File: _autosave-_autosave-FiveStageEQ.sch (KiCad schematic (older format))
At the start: 75 parts, among them J1 AudioJack3, J2 AudioJack3, U1 LM833, U2 LM833, U3 LM833, U4 LM833, U5 LM833, U6 LM833, U7 LM833, U8 LM317_TO3

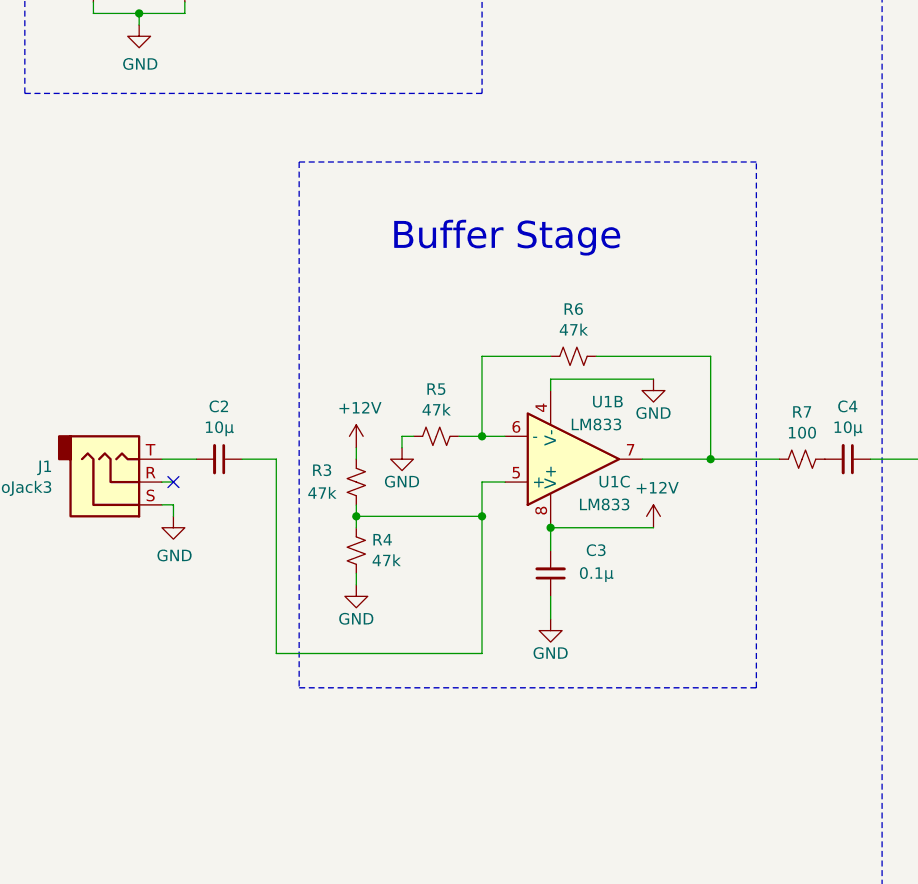
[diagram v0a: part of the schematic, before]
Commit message: Corrected schematic
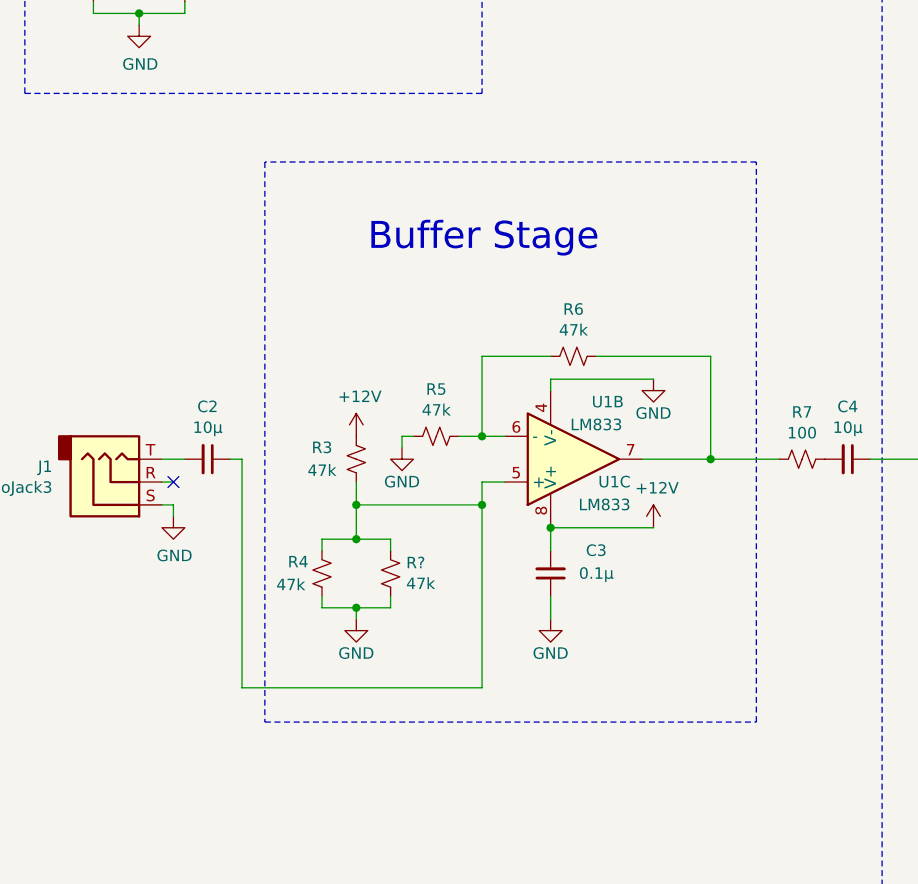
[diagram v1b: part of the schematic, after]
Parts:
- added R?: 47k, Resistor_SMD:R_0603_1608Metric, symbol FiveStageEQ-rescue:R_Small_US-Device
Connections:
- net GND: now also R?.1
- net at C2.1, R3.2, R4.2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: now also R?.2
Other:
- moved on the sheet: C2, R3, R4

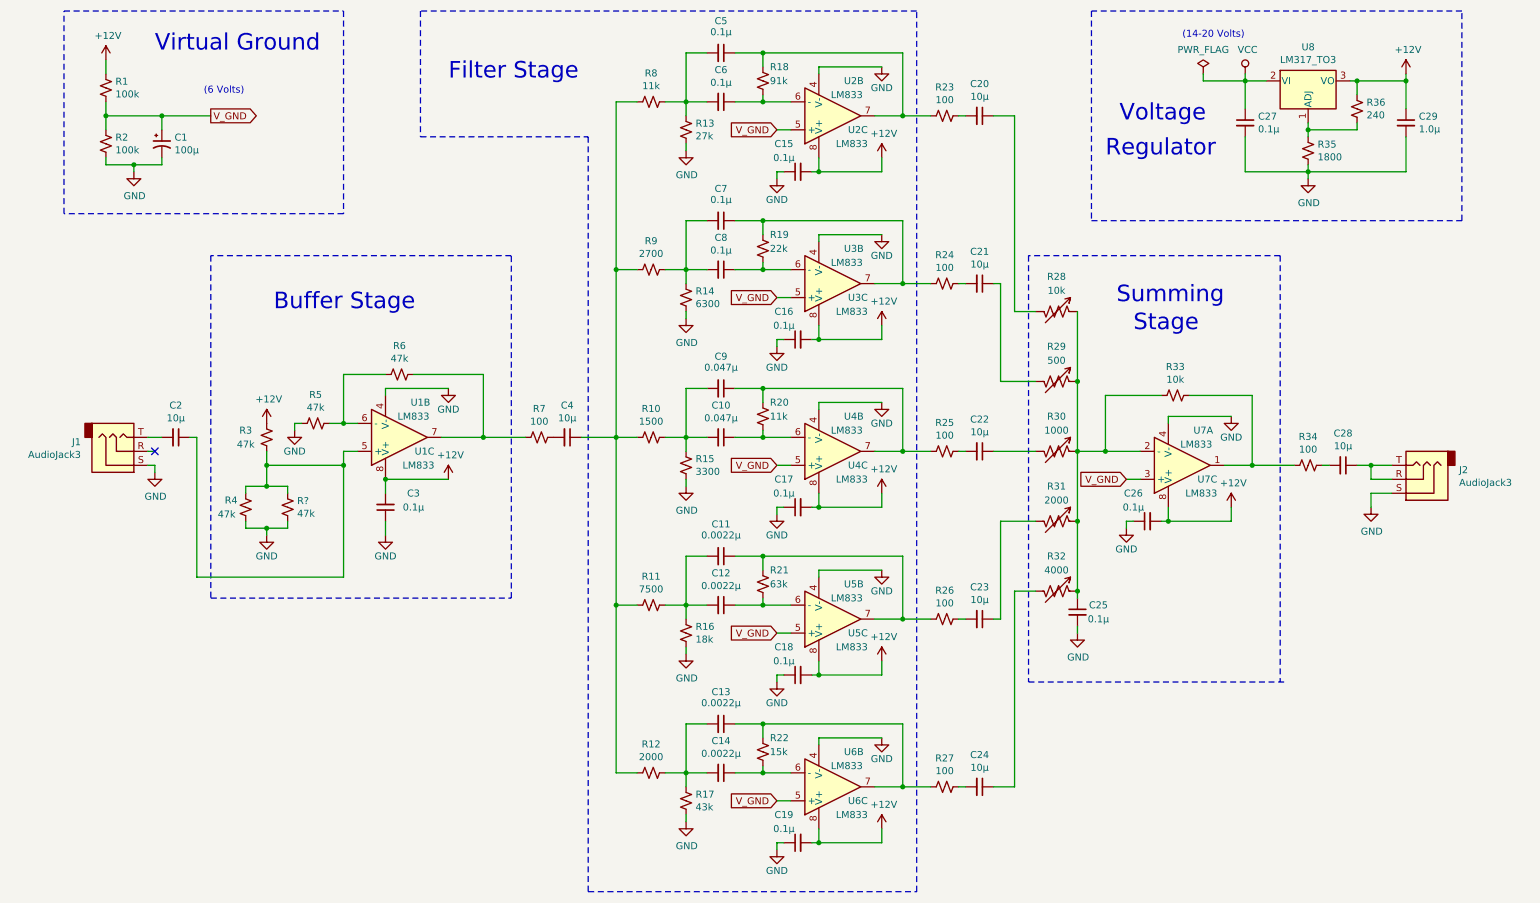
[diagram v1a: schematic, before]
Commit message: added poster of EQ
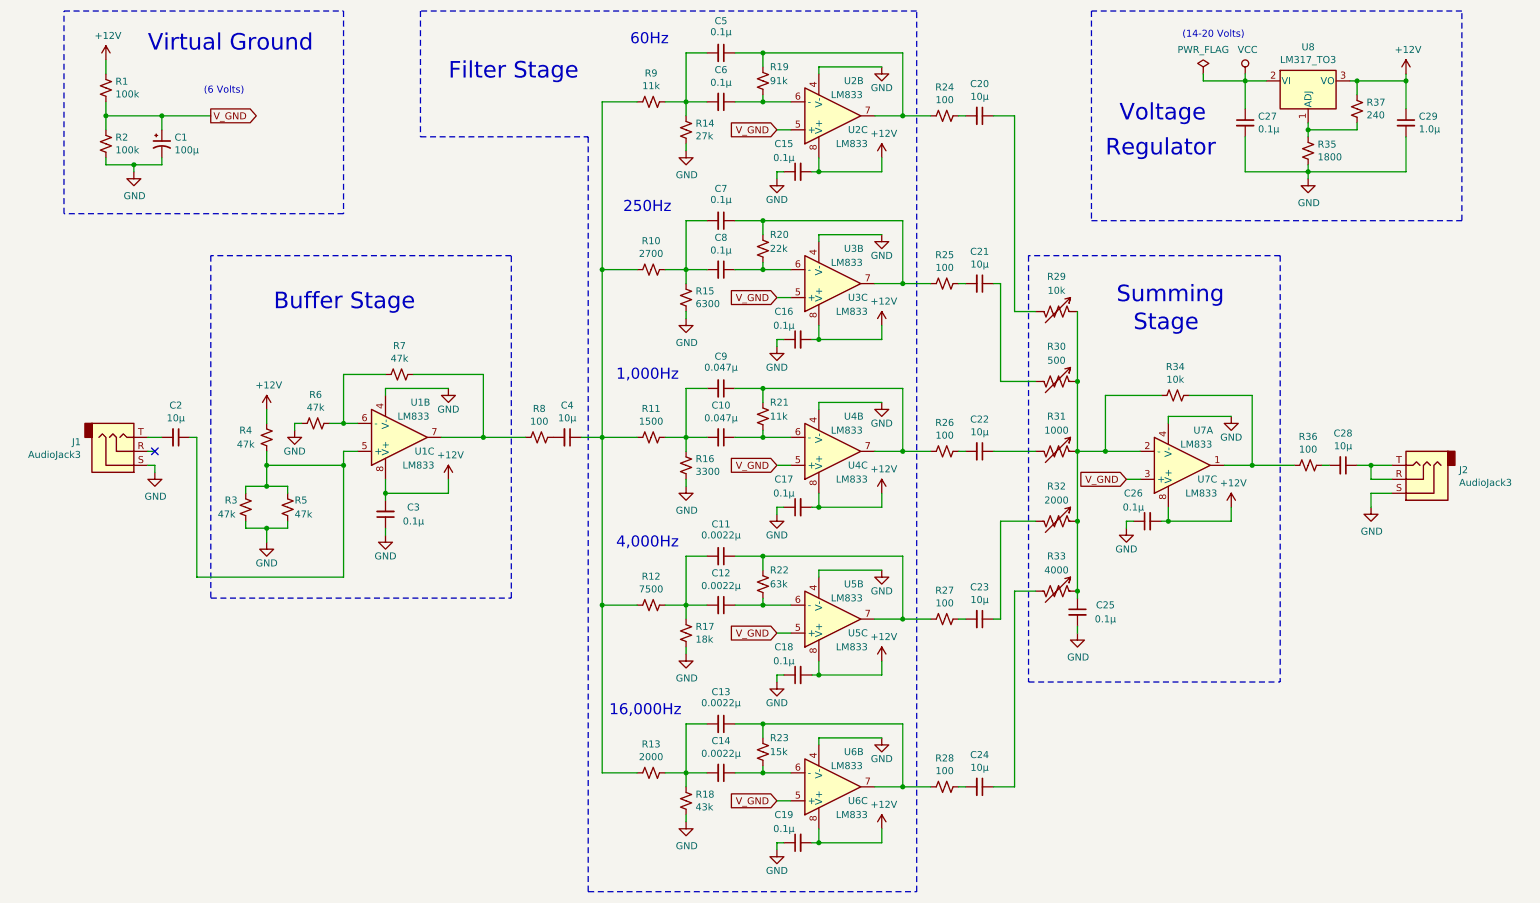
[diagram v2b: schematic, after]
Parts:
- removed R?: 47k, Resistor_SMD:R_0603_1608Metric, symbol FiveStageEQ-rescue:R_Small_US-Device
- added R5: 47k, Resistor_SMD:R_0603_1608Metric, symbol FiveStageEQ-rescue:R_Small_US-Device
- renumbered R9 to R10, R10 to R11, R11 to R12, R12 to R13, R13 to R14, R14 to R15, R15 to R16, R16 to R17, R17 to R18, R18 to R19, R19 to R20, R20 to R21, R21 to R22, R22 to R23, R23 to R24, R24 to R25, R25 to R26, R26 to R27, R27 to R28, R28 to R29, R4 to R3, R29 to R30, R30 to R31, R31 to R32, R32 to R33, R33 to R34, R34 to R36, R36 to R37, R3 to R4, R5 to R6, R6 to R7, R7 to R8, R8 to R9
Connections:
- net GND: now also R5.1
- net at C2.1, R3.2, R4.2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: now also R5.2
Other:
- note added: "1,000Hz"
- note added: "16,000Hz"
- note added: "250Hz"
- note added: "4,000Hz"
- note added: "60Hz"
- moved on the sheet: C3

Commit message: added PCB design and made some adjustments to schematic to accomodate footprints
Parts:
- removed C16, C18: 0.1μ, Capacitor_SMD:C_0603_1608Metric, symbol FiveStageEQ-rescue:C_Small-Device
- removed J1, J2: AudioJack3, Connector_Audio:Jack_3.5mm_CUI_SJ-3523-SMT_Horizontal, symbol FiveStageEQ-rescue:AudioJack3-Connector
- removed R29: 10k, Potentiometer_THT:Potentiometer_Vishay_148-149_Single_Vertical, symbol FiveStageEQ-rescue:R_Variable_US-Device
- removed R30: 500, Potentiometer_THT:Potentiometer_Vishay_148-149_Single_Vertical, symbol FiveStageEQ-rescue:R_Variable_US-Device
- removed R31: 1000, Potentiometer_THT:Potentiometer_Vishay_148-149_Single_Vertical, symbol FiveStageEQ-rescue:R_Variable_US-Device
- removed R32: 2000, Potentiometer_THT:Potentiometer_Vishay_148-149_Single_Vertical, symbol FiveStageEQ-rescue:R_Variable_US-Device
- removed R33: 4000, Potentiometer_THT:Potentiometer_Vishay_148-149_Single_Vertical, symbol FiveStageEQ-rescue:R_Variable_US-Device
- removed unit 3 of U3
- removed unit 3 of U5
- added J1, J2: AudioJack3, SJ1-3523N:CUI_SJ1-3523N, symbol Connector:AudioJack3
- added R29: 10k, SamacSys_Parts:PTV09A4015FA103, symbol Device:R_Potentiometer_US
- added R30: 500, SamacSys_Parts:PCW1DC24BAB501L, symbol Device:R_Potentiometer_US
- added R31: 1000, SamacSys_Parts:PTV09A4015FB103, symbol Device:R_Potentiometer_US
- added R32: 2000, SamacSys_Parts:PTV09A4020FB503, symbol Device:R_Potentiometer_US
- added R33: 4000, SamacSys_Parts:PTV09A4020FB103, symbol Device:R_Potentiometer_US
- C1: footprint Capacitor_SMD:C_0603_1608Metric -> 100uf_cap:FK20X5R0J107M
- C10, C9: footprint Capacitor_SMD:C_0603_1608Metric -> SamacSys_Parts:CAPC1005X55N
- C11, C12, C13, C14: footprint Capacitor_SMD:C_0603_1608Metric -> SamacSys_Parts:CAPC0603X33N
- C15, C3, C5, C6, C7, C8: footprint Capacitor_SMD:C_0603_1608Metric -> SamacSys_Parts:CAPPA1472W54L508D241
- C16: renamed from C17; footprint Capacitor_SMD:C_0603_1608Metric -> SamacSys_Parts:CAPPA1472W54L508D241
- C17: renamed from C19; footprint Capacitor_SMD:C_0603_1608Metric -> SamacSys_Parts:CAPPA1472W54L508D241
- C18: renamed from C20; footprint Capacitor_SMD:C_0603_1608Metric -> SamacSys_Parts:RCE5C1H104J2A2H03B
- C19: renamed from C21; footprint Capacitor_SMD:C_0603_1608Metric -> SamacSys_Parts:RCE5C1H104J2A2H03B
- C2, C4: footprint Capacitor_SMD:C_0603_1608Metric -> SamacSys_Parts:RCE5C1H104J2A2H03B
- C20: renamed from C22; footprint Capacitor_SMD:C_0603_1608Metric -> SamacSys_Parts:RCE5C1H104J2A2H03B
- C21: renamed from C23; footprint Capacitor_SMD:C_0603_1608Metric -> SamacSys_Parts:RCE5C1H104J2A2H03B
- C22: renamed from C24; footprint Capacitor_SMD:C_0603_1608Metric -> SamacSys_Parts:RCE5C1H104J2A2H03B
- C23: renamed from C25; footprint Capacitor_SMD:C_0603_1608Metric -> SamacSys_Parts:CAPPA1472W54L508D241
- C24: renamed from C26; footprint Capacitor_SMD:C_0603_1608Metric -> SamacSys_Parts:CAPPA1472W54L508D241
- C25: renamed from C27; footprint Capacitor_SMD:C_0603_1608Metric -> SamacSys_Parts:CAPPA1472W54L508D241
- C26: renamed from C28; footprint Capacitor_SMD:C_0603_1608Metric -> SamacSys_Parts:RCE5C1H104J2A2H03B
- C27: renamed from C29; footprint Capacitor_SMD:C_0603_1608Metric -> SamacSys_Parts:C330C105K5R5TA
- R1, R10, R13, R14, R2, R22, R35: footprint Resistor_SMD:R_0603_1608Metric -> SamacSys_Parts:RESC2012X60N
- R11, R12, R15, R16, R18, R19, R20, R21, R23, R34, R37: footprint Resistor_SMD:R_0603_1608Metric -> SamacSys_Parts:RESC1608X55N
- R17: footprint Resistor_SMD:R_0603_1608Metric -> footprints:CFR-25JB-52-18K
- R24, R25, R26, R27, R28, R36, R8: footprint Resistor_SMD:R_0603_1608Metric -> SamacSys_Parts:RESAD2990W85L1150D460
- R3, R4, R5, R6, R7: footprint Resistor_SMD:R_0603_1608Metric -> footprints:RN73R1ETTP2001D25
- R9: footprint Resistor_SMD:R_0603_1608Metric -> SamacSys_Parts:RCE5C1H104J2A2H03B
- U1, U2: footprint (none) -> LM833_Badge:LM833-N-PDIP
- U2: renamed from U3; footprint (none) -> LM833_Badge:LM833-N-PDIP
- U3: renamed from U4; footprint (none) -> LM833_Badge:LM833-N-PDIP
- U3: renamed from U5; footprint (none) -> LM833_Badge:LM833-N-PDIP
- U4: renamed from U6; footprint (none) -> LM833_Badge:LM833-N-PDIP
- U5: renamed from U7; footprint (none) -> LM833_Badge:LM833-N-PDIP
- U6: renamed from U8; value LM317_TO3 -> LM317_T; footprint Package_TO_SOT_THT:TO-220-3_Horizontal_TabDown -> SamacSys_Parts:TO255P460X1020X2008-3P
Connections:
- net GND: now also J1.1 (S), J2.1 (S)
- net V_GND: now also U2.3 (+), U3.3 (+); no longer U2.5 (+), U3.5 (+)
- net at C6.1, R19.1: now also U2.2 (-); no longer U2.6 (-)
- net at C5.1, R19.2, R24.1: now also U2.1; no longer U2.7
- net at C18.1: now also R29.3
- net at C23.1, R34.1, U5.2 (-): now also R29.1, R30.1, R31.1, R32.1, R33.1
- net at C2.2: now also J1.2 (T)
- net at C26.1: now also J2.2 (T), J2.3 (R)
- net at C2.1, R3.2, R4.2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: now also U1.3 (+); no longer U1.5 (+)
- net at R6.2, R7.1: now also U1.2 (-); no longer U1.6 (-)
- net at R7.2, R8.1: now also U1.1; no longer U1.7
- net at C19.1: now also R30.3
- net at C9.1, R21.2, R26.1: now also U3.1; no longer U3.7
- net at C10.1, R21.1: now also U3.2 (-); no longer U3.6 (-)
- net at C20.1: now also R31.3
- net at C21.1: now also R32.3
- net at C22.1: now also R33.3
